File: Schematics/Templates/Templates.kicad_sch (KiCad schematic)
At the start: 4 parts, among them J1 Stack Male Edge Connector, J2 Stack Female Edge Connector, J3 SWD_01x04_Pin, U1 SAM-M8Q

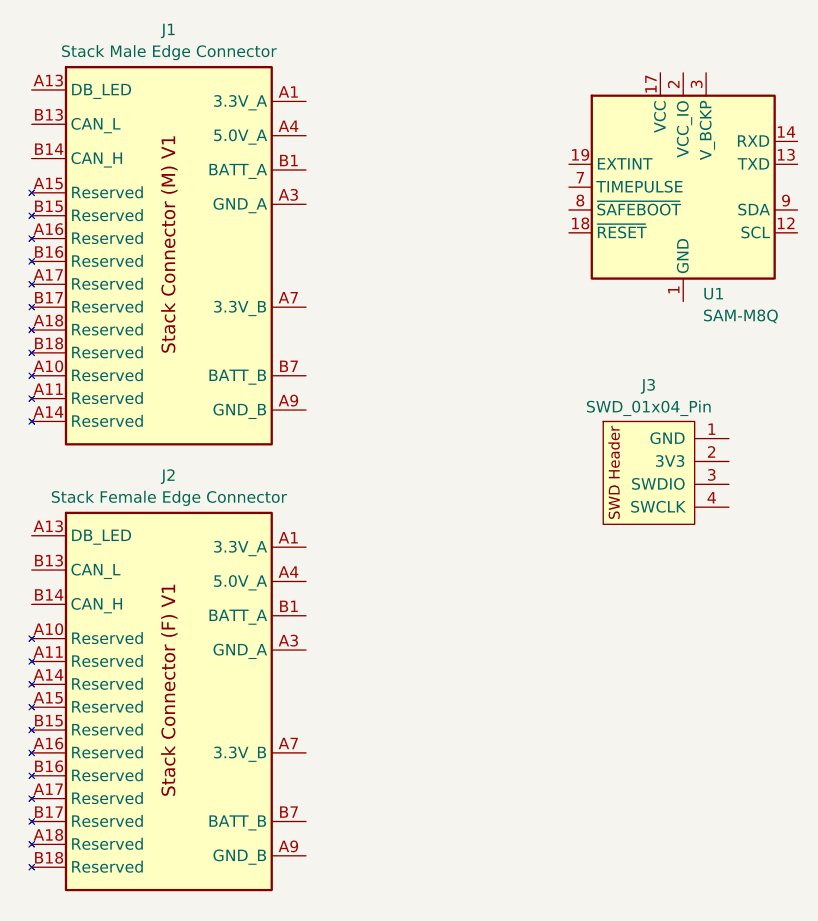
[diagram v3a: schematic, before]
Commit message: Fixed misnamed "5.5V" pin
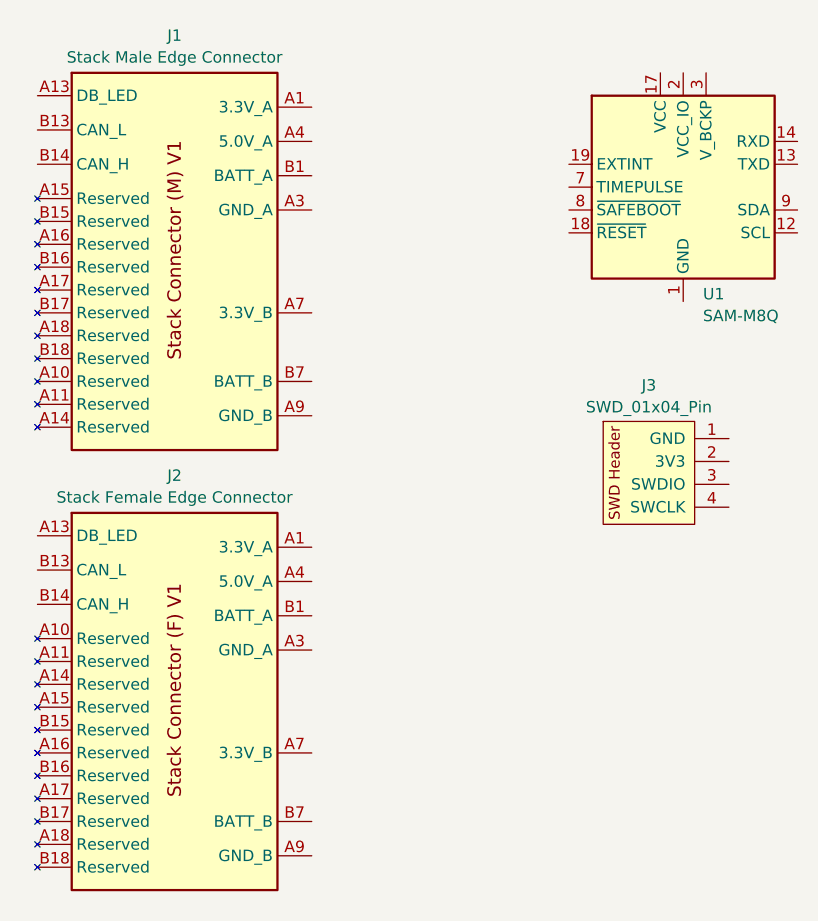
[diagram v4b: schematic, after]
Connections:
- net 5.5V_A renamed 5.0V_A
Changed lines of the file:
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@@
 (kicad_sch (version 20230121) (generator eeschema)
   (paper "A4")
-  (symbol (lib_id "EdgeConnector:Stack Female Edge Connector") (at 50.8 94.615 0) (unit 1)
-    (in_bom yes) (on_board yes) (dnp no) (fields_autoplaced)
-    (property "Reference" "J2" (at 50.8 68.8807 0)
-      (effects (font (size 1.27 1.27)))
-    )
-    (property "Value" "Stack Female Edge Connector" (at 50.8 71.3049 0)
-      (effects (font (size 1.27 1.27)))
-    )
-    (property "Footprint" "footprints:AMPHENOL_10018784-10210TLF" (at 50.8 117.475 0)
-      (effects (font (size 1.27 1.27)) hide)
-    )
-    (property "Datasheet" "" (at 44.45 113.665 0)
-      (effects (font (size 1.27 1.27)) hide)
-    )
-    (pin "A1")
-    (pin "A10")
-    (pin "A11")
-    (pin "A12")
-    (pin "A13")
-    (pin "A14")
-    (pin "A15")
-    (pin "A16")
-    (pin "A17")
-    (pin "A18")
-    (pin "A2")
-    (pin "A3")
-    (pin "A4")
-    (pin "A5")
-    (pin "A6")
-    (pin "A7")
-    (pin "A8")
-    (pin "A9")
-    (pin "B1")
-    (pin "B10")
-    (pin "B11")
-    (pin "B12")
-    (pin "B13")
-    (pin "B14")
-    (pin "B15")
-    (pin "B16")
-    (pin "B17")
-    (pin "B18")
-    (pin "B2")
-    (pin "B3")
-    (pin "B4")
-    (pin "B5")
-    (pin "B6")
-    (pin "B7")
-    (pin "B8")
-    (pin "B9")
-    (instances
-      (project "Templates"
-        (path "/89e89115-178c-4161-95c1-6f6deb6f4aa1"
-          (reference "J2") (unit 1)
-        )
-      )
-    )
-  )
   (symbol (lib_id "EdgeConnector:SWD_01x04_Pin") (at 107.95 67.31 0) (unit 1)
     (in_bom yes) (on_board yes) (dnp no) (fields_autoplaced)
@@
     )
   )
-  (symbol (lib_name "Stack Male Edge Connector_1") (lib_id "EdgeConnector:Stack Male Edge Connector") (at 50.8 45.085 0) (unit 1)
+  (symbol (lib_id "EdgeConnector:Stack Male Edge Connector") (at 51.435 45.72 0) (unit 1)
     (in_bom yes) (on_board yes) (dnp no) (fields_autoplaced)
-    (property "Reference" "J1" (at 50.8 19.3507 0)
+    (property "Reference" "J1" (at 51.435 19.9857 0)
       (effects (font (size 1.27 1.27)))
     )
-    (property "Value" "Stack Male Edge Connector" (at 50.8 21.7749 0)
+    (property "Value" "Stack Male Edge Connector" (at 51.435 22.4099 0)
       (effects (font (size 1.27 1.27)))
     )
-    (property "Footprint" "Connector_PCBEdge:BUS_PCIexpress_x1" (at 50.8 67.945 0)
+    (property "Footprint" "Connector_PCBEdge:BUS_PCIexpress_x1" (at 51.435 68.58 0)
       (effects (font (size 1.27 1.27)) hide)
     )
-    (property "Datasheet" "" (at 44.45 64.135 0)
+    (property "Datasheet" "" (at 45.085 64.77 0)
       (effects (font (size 1.27 1.27)) hide)
     )
@@
         )
       )
+    )
+  )
+  (symbol (lib_id "EdgeConnector:Stack Female Edge Connector") (at 51.435 94.615 0) (unit 1)
+    (in_bom yes) (on_board yes) (dnp no) (fields_autoplaced)
+    (property "Reference" "J2" (at 51.435 68.8807 0)
+      (effects (font (size 1.27 1.27)))
+    )
+    (property "Value" "Stack Female Edge Connector" (at 51.435 71.3049 0)
+      (effects (font (size 1.27 1.27)))
+    )
+    (property "Footprint" "footprints:AMPHENOL_10018784-10210TLF" (at 51.435 117.475 0)
+      (effects (font (size 1.27 1.27)) hide)
+    )
+    (property "Datasheet" "" (at 45.085 113.665 0)
+      (effects (font (size 1.27 1.27)) hide)
+    )
+    (pin "A1")
+    (pin "A10")
+    (pin "A11")
+    (pin "A12")
+    (pin "A13")
+    (pin "A14")
+    (pin "A15")
+    (pin "A16")
+    (pin "A17")
+    (pin "A18")
+    (pin "A2")
+    (pin "A3")
+    (pin "A4")
+    (pin "A5")
+    (pin "A6")
+    (pin "A7")
+    (pin "A8")
+    (pin "A9")
+    (pin "B1")
+    (pin "B10")
+    (pin "B11")
+    (pin "B12")
+    (pin "B13")
+    (pin "B14")
+    (pin "B15")
+    (pin "B16")
+    (pin "B17")
+    (pin "B18")
+    (pin "B2")
+    (pin "B3")
+    (pin "B4")
+    (pin "B5")
+    (pin "B6")
+    (pin "B7")
+    (pin "B8")
+    (pin "B9")
+    (instances
+      (project "Templates"
+        (path "/89e89115-178c-4161-95c1-6f6deb6f4aa1"
+          (reference "J2") (unit 1)
+        )
+      )
